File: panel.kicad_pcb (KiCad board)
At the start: 2 copper layers, 96.5 x 72.1 mm, 50 parts, among them J1 Conn_01x05, J2 Conn_01x05, J3 Conn_01x05, J4 Conn_01x05, J5 Regulator connector, J6 JST_SH_SM06B-SRSS-TB_1x06-1MP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, J7 Conn_01x04, U1 M24C02-FMN

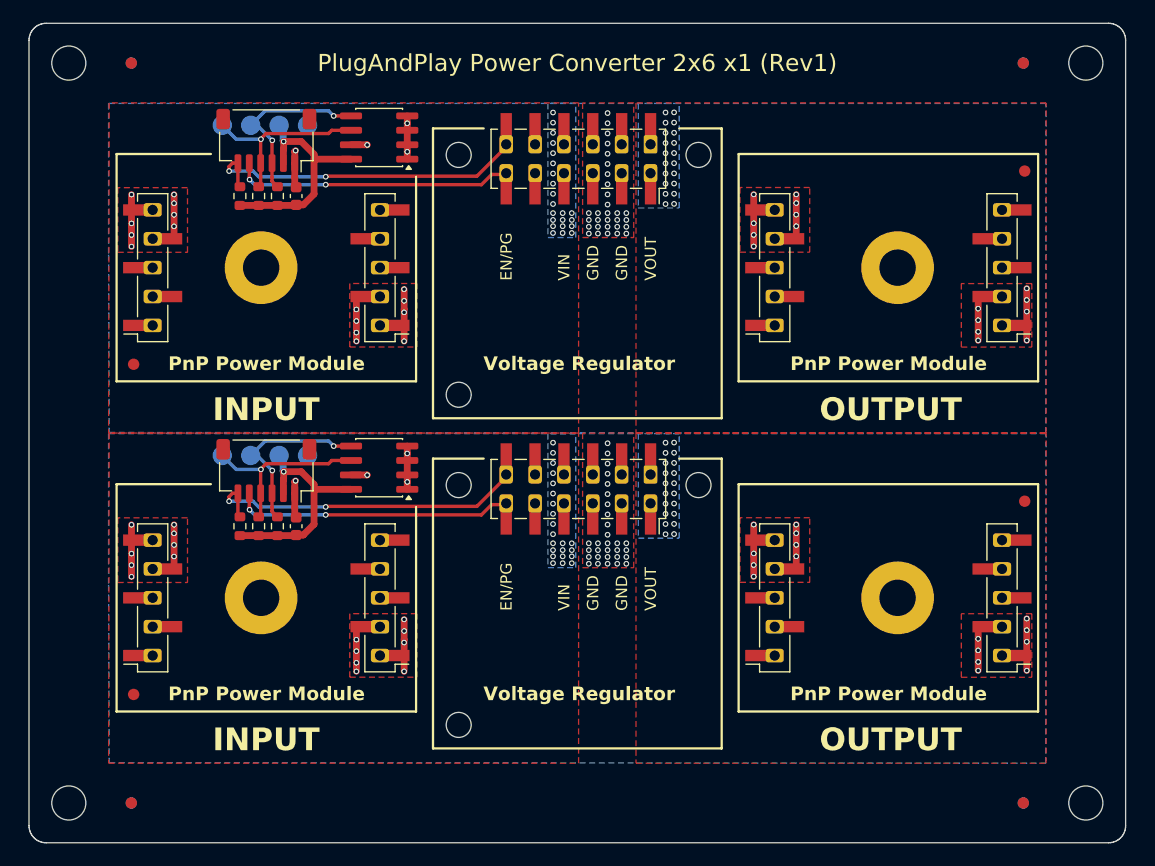
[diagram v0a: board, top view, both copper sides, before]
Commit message: Rotate regulator 90deg to have better connection to VIN and VOUT lines
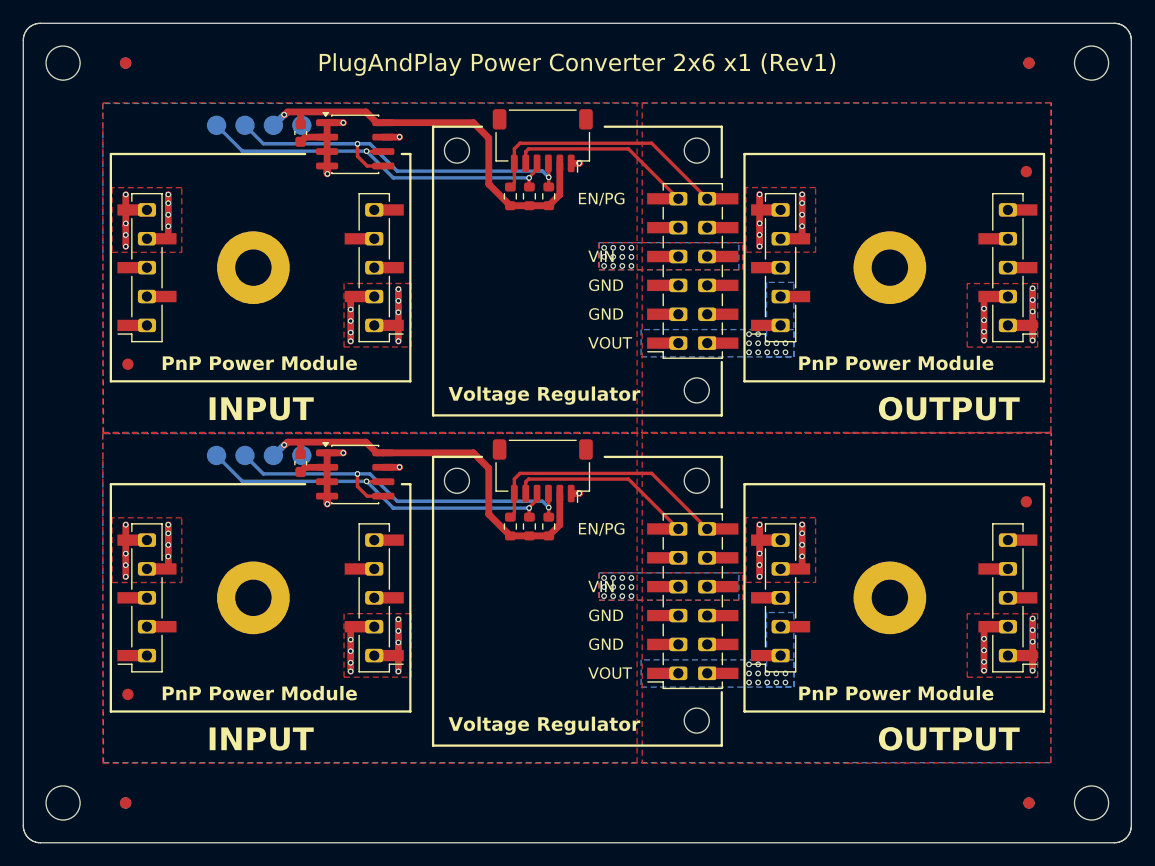
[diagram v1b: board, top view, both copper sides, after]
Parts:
- removed the C1 at (123.8, 35.2)
- removed the C1 at (123.8, 64.2)
- removed the J1 at (111.1, 41.5)
- removed the J1 at (111.1, 70.5)
- removed the J2 at (131.1, 41.5)
- removed the J2 at (131.1, 70.5)
- removed the J3 at (165.9, 41.5)
- removed the J3 at (165.9, 70.5)
- removed the J4 at (185.9, 70.5)
- removed the J4 at (185.9, 41.5)
- removed the J5 at (148.6, 31.9)
- removed the J5 at (148.6, 61.0)
- removed the J6 at (121.1, 59.4)
- removed the J6 at (121.1, 30.3)
- removed the J7 at (124.8, 29.0)
- removed the J7 at (124.8, 58.0)
- removed the R1 at (122.1, 35.2)
- removed the R1 at (122.1, 64.2)
- removed the R2 at (120.5, 35.2)
- removed the R2 at (120.5, 64.2)
- removed the R3 at (118.8, 35.2)
- removed the R3 at (118.8, 64.2)
- removed the REF** at (159.2, 60.6)
- removed the REF** at (187.9, 33.0)
- removed the REF** at (159.2, 31.6)
- removed the REF** at (109.5, 50.0)
- removed the REF** at (176.7, 41.5)
- removed the REF** at (138.1, 81.7)
- removed the REF** at (120.7, 70.5)
- removed the REF** at (138.1, 52.7)
- removed the REF** at (176.7, 70.5)
- removed the REF** at (187.9, 62.0)
- removed the REF** at (109.5, 79.0)
- removed the REF** at (138.1, 31.6)
- removed the REF** at (138.1, 60.6)
- removed the REF** at (120.7, 41.5)
- removed the U1 at (131.1, 30.1)
- removed the U1 at (131.1, 59.1)
- added C1: 0.1uF, Capacitor_SMD:C_0603_1608Metric, F.Cu at (124.2, 58.7)
- added C1: 0.1uF, Capacitor_SMD:C_0603_1608Metric, F.Cu at (124.2, 29.6)
- added J1: Conn_01x05, PnP_Library:PinSocket_1x05_P2.54mm_Vertical_SMD_Pin1Right, F.Cu at (110.6, 70.5)
- added J1: Conn_01x05, PnP_Library:PinSocket_1x05_P2.54mm_Vertical_SMD_Pin1Right, F.Cu at (110.6, 41.5)
- added J2: Conn_01x05, PnP_Library:PinSocket_1x05_P2.54mm_Vertical_SMD_Pin1Left, F.Cu at (130.6, 41.5)
- added J2: Conn_01x05, PnP_Library:PinSocket_1x05_P2.54mm_Vertical_SMD_Pin1Left, F.Cu at (130.6, 70.5)
- added J3: Conn_01x05, PnP_Library:PinSocket_1x05_P2.54mm_Vertical_SMD_Pin1Right, F.Cu at (166.4, 41.5)
- added J3: Conn_01x05, PnP_Library:PinSocket_1x05_P2.54mm_Vertical_SMD_Pin1Right, F.Cu at (166.4, 70.5)
- added J4: Conn_01x05, PnP_Library:PinSocket_1x05_P2.54mm_Vertical_SMD_Pin1Left, F.Cu at (186.4, 70.5)
- added J4: Conn_01x05, PnP_Library:PinSocket_1x05_P2.54mm_Vertical_SMD_Pin1Left, F.Cu at (186.4, 41.5)
- added J5: Regulator connector, PnP_Library:PinSocket_2x06_P2.54mm_Vertical_SMD, F.Cu at (158.7, 41.8)
- added J5: Regulator connector, PnP_Library:PinSocket_2x06_P2.54mm_Vertical_SMD, F.Cu at (158.7, 70.8)
- added J6: JST_SH_SM06B-SRSS-TB_1x06-1MP_P1.00mm_Horizontal, Connector_JST:JST_SH_SM06B-SRSS-TB_1x06-1MP_P1.00mm_Horizontal, F.Cu at (145.5, 30.3)
- added J6: JST_SH_SM06B-SRSS-TB_1x06-1MP_P1.00mm_Horizontal, Connector_JST:JST_SH_SM06B-SRSS-TB_1x06-1MP_P1.00mm_Horizontal, F.Cu at (145.5, 59.4)
- added J7: Conn_01x04, PnP_Library:PogoPinsPads_1x04_P2.5mm, B.Cu at (124.3, 58.0)
- added J7: Conn_01x04, PnP_Library:PogoPinsPads_1x04_P2.5mm, B.Cu at (124.3, 29.0)
- added R1: 2.2K, Resistor_SMD:R_0603_1608Metric, F.Cu at (146.0, 64.3)
- added R1: 2.2K, Resistor_SMD:R_0603_1608Metric, F.Cu at (146.0, 35.2)
- added R2: 2.2K, Resistor_SMD:R_0603_1608Metric, F.Cu at (144.3, 35.2)
- added R2: 2.2K, Resistor_SMD:R_0603_1608Metric, F.Cu at (144.3, 64.3)
- added R3: 100K, Resistor_SMD:R_0603_1608Metric, F.Cu at (142.6, 64.3)
- added R3: 100K, Resistor_SMD:R_0603_1608Metric, F.Cu at (142.6, 35.2)
- added REF**: MountingHole_2.2mm_M2, MountingHole:MountingHole_2.2mm_M2, F.Cu at (159.0, 52.3)
- added REF**: Fiducial_1mm_Mask2mm, Fiducial:Fiducial_1mm_Mask2mm, F.Cu at (109.0, 79.0)
- added REF**: MountingHole_3.2mm_M3_Pad, MountingHole:MountingHole_3.2mm_M3_Pad, F.Cu at (120.0, 70.5)
- added REF**: MountingHole_3.2mm_M3_Pad, MountingHole:MountingHole_3.2mm_M3_Pad, F.Cu at (176.0, 41.5)
- added REF**: MountingHole_2.2mm_M2, MountingHole:MountingHole_2.2mm_M2, F.Cu at (159.0, 81.3)
- added REF**: MountingHole_2.2mm_M2, MountingHole:MountingHole_2.2mm_M2, F.Cu at (137.9, 60.2)
- added REF**: MountingHole_3.2mm_M3_Pad, MountingHole:MountingHole_3.2mm_M3_Pad, F.Cu at (176.0, 70.5)
- added REF**: Fiducial_1mm_Mask2mm, Fiducial:Fiducial_1mm_Mask2mm, F.Cu at (188.0, 33.0)
- added REF**: MountingHole_3.2mm_M3_Pad, MountingHole:MountingHole_3.2mm_M3_Pad, F.Cu at (120.0, 41.5)
- added REF**: MountingHole_2.2mm_M2, MountingHole:MountingHole_2.2mm_M2, F.Cu at (137.9, 31.2)
- added REF**: Fiducial_1mm_Mask2mm, Fiducial:Fiducial_1mm_Mask2mm, F.Cu at (188.0, 62.1)
- added REF**: Fiducial_1mm_Mask2mm, Fiducial:Fiducial_1mm_Mask2mm, F.Cu at (109.0, 50.0)
- added REF**: MountingHole_2.2mm_M2, MountingHole:MountingHole_2.2mm_M2, F.Cu at (159.0, 31.2)
- added REF**: MountingHole_2.2mm_M2, MountingHole:MountingHole_2.2mm_M2, F.Cu at (159.0, 60.2)
- added U1: M24C02-FMN, Package_SO:SOIC-8_3.9x4.9mm_P1.27mm, F.Cu at (129.0, 59.7)
- added U1: M24C02-FMN, Package_SO:SOIC-8_3.9x4.9mm_P1.27mm, F.Cu at (129.0, 30.6)
- moved KiKit_FID_B_1 0.50 mm to (108.8, 23.5)
- moved KiKit_FID_B_2 0.50 mm to (188.2, 23.5)
- moved KiKit_FID_B_3 0.50 mm to (108.8, 88.6)
- moved KiKit_FID_B_4 0.50 mm to (188.2, 88.6)
- moved KiKit_FID_T_1 0.50 mm to (108.8, 23.5)
- moved KiKit_FID_T_2 0.50 mm to (188.2, 23.5)
- moved KiKit_FID_T_3 0.50 mm to (108.8, 88.6)
- moved KiKit_FID_T_4 0.50 mm to (188.2, 88.6)
- moved KiKit_TO_1 0.50 mm to (103.3, 23.5)
- moved KiKit_TO_2 0.50 mm to (193.7, 23.5)
- moved KiKit_TO_3 0.50 mm to (103.3, 88.6)
- moved KiKit_TO_4 0.50 mm to (193.7, 88.6)
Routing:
- net Board_1-SDA: track 16.3 -> 34.4 mm
- net Board_0-SDA: track 16.3 -> 34.4 mm
- net Board_1-SCL: track 16.5 -> 33.3 mm, vias 1 -> 2
- net Board_0-SCL: track 16.5 -> 33.3 mm, vias 1 -> 2
- net Board_0-VCC: track 20.9 -> 35.4 mm
- net Board_1-VCC: track 20.9 -> 35.4 mm
- net Board_0-EN/INT1: track 24.6 -> 16.4 mm, vias 2 -> 0
- net Board_1-EN/INT1: track 24.6 -> 16.4 mm, vias 2 -> 0
- net Board_0-PG/INT2: track 29.7 -> 22.7 mm, vias 2 -> 0
- net Board_1-PG/INT2: track 29.7 -> 22.7 mm, vias 2 -> 0
- net Board_0-GND: track 46.8 -> 50.2 mm, vias 66 -> 36
- net Board_1-GND: track 46.8 -> 50.2 mm, vias 66 -> 36
- net Board_1-VOUT: track 1.11 -> 0.35 mm, vias 20 -> 12
- net Board_1-VIN: track 0.76 -> 0.00 mm, vias 22 -> 12
- net Board_0-VOUT: track 1.11 -> 0.35 mm, vias 20 -> 12
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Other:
- board size 96.5 x 72.1 mm -> 97.5 x 72.1 mm
- board text added: "Plug-n-Play Power Converter 1x6 x1"
- board text removed: "Plug-n-Play Power Converter 2x6 x1"
